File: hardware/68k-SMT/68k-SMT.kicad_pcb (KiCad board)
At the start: 2 copper layers, 106.7 x 139.7 mm, 67 parts, among them J1 ADBUS, J3 SIGBUS, J4 Serial1, J5 Serial2, J6 CompactFlash, SW1 RESET, SW2 IP2, SW3 IP3, U1 74HC32, U10 HM628512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

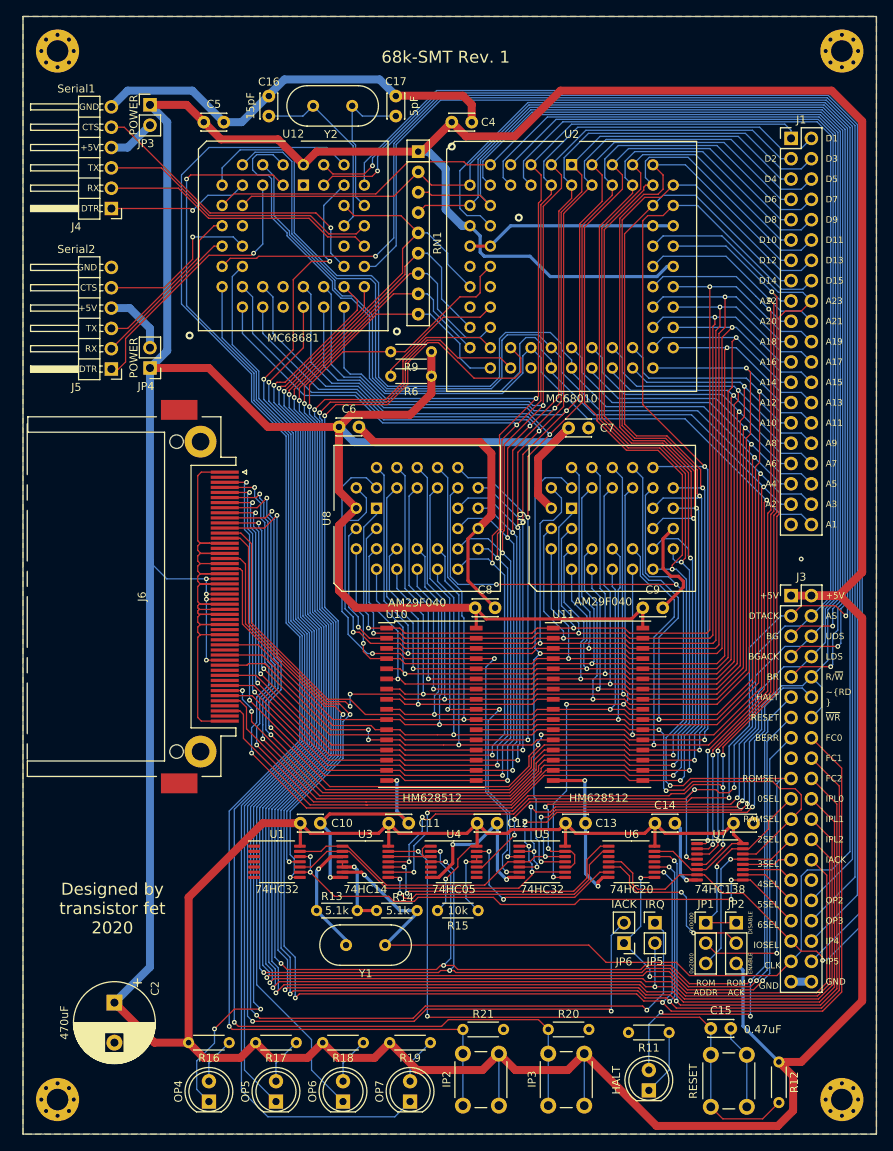
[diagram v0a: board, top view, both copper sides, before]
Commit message: Removed IDE header which doesn't easily fit, and cleaned up the PCB design a bit
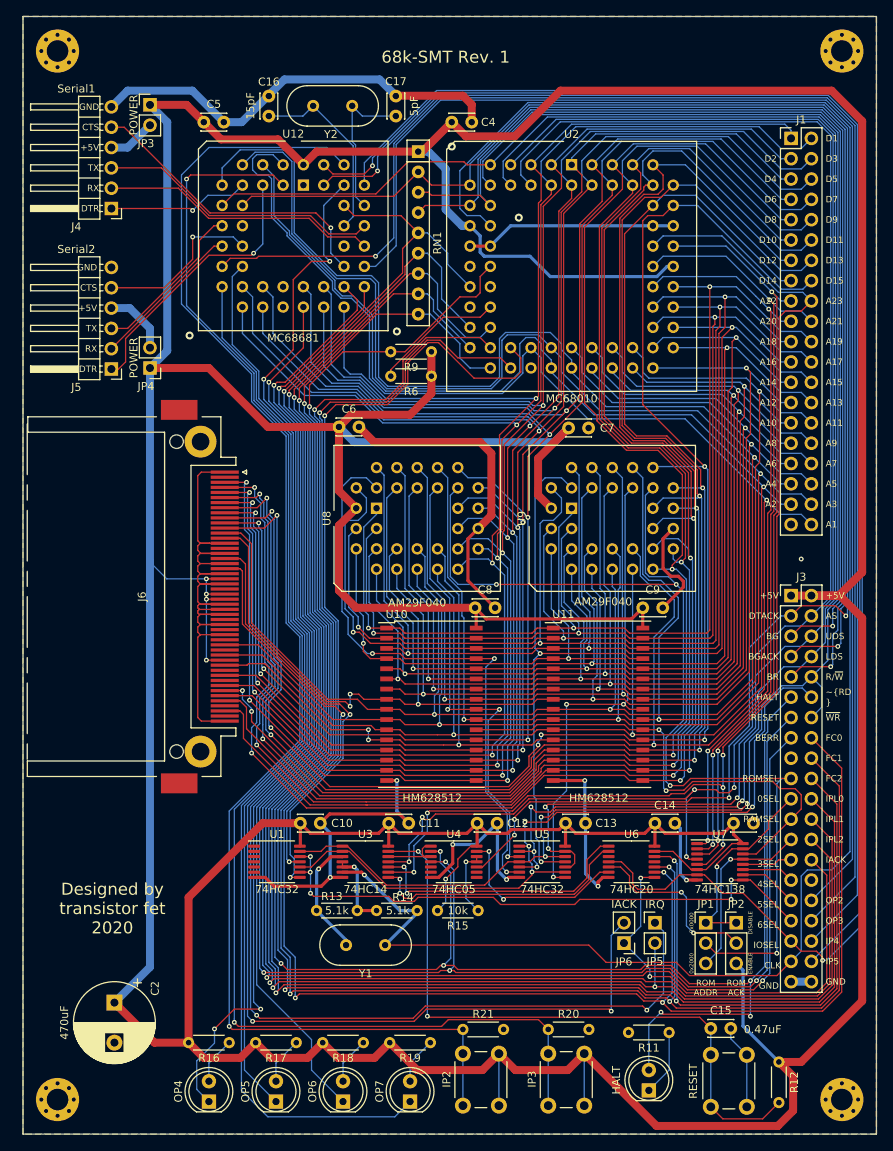
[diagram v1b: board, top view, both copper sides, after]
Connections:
- J6 pad 32: A12 -> A5
- J6 pad 7: A11 -> A4
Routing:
- net A11: track 216.6 -> 171.3 mm
- net A12: track 199.8 -> 156.3 mm, vias 5 -> 3
- net A5: track 155.8 -> 192.1 mm, vias 3 -> 5
- net A4: track 227.1 -> 262.3 mm
- net GND: track 314.7 -> 325.1 mm
- net 6SEL: track 71.6 -> 73.1 mm, vias 4 -> 5
- net D11: track 217.5 -> 218.6 mm
- net D9: track 182.0 -> 183.1 mm
- net D5: track 227.6 -> 228.4 mm
- net D7: track 224.7 -> 225.5 mm
- net D4: track 220.5 -> 221.2 mm
- net D10: track 183.2 -> 183.8 mm
- net D1: track 200.0 -> 200.5 mm

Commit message: Finalized 68k-SMT board and sent off to print
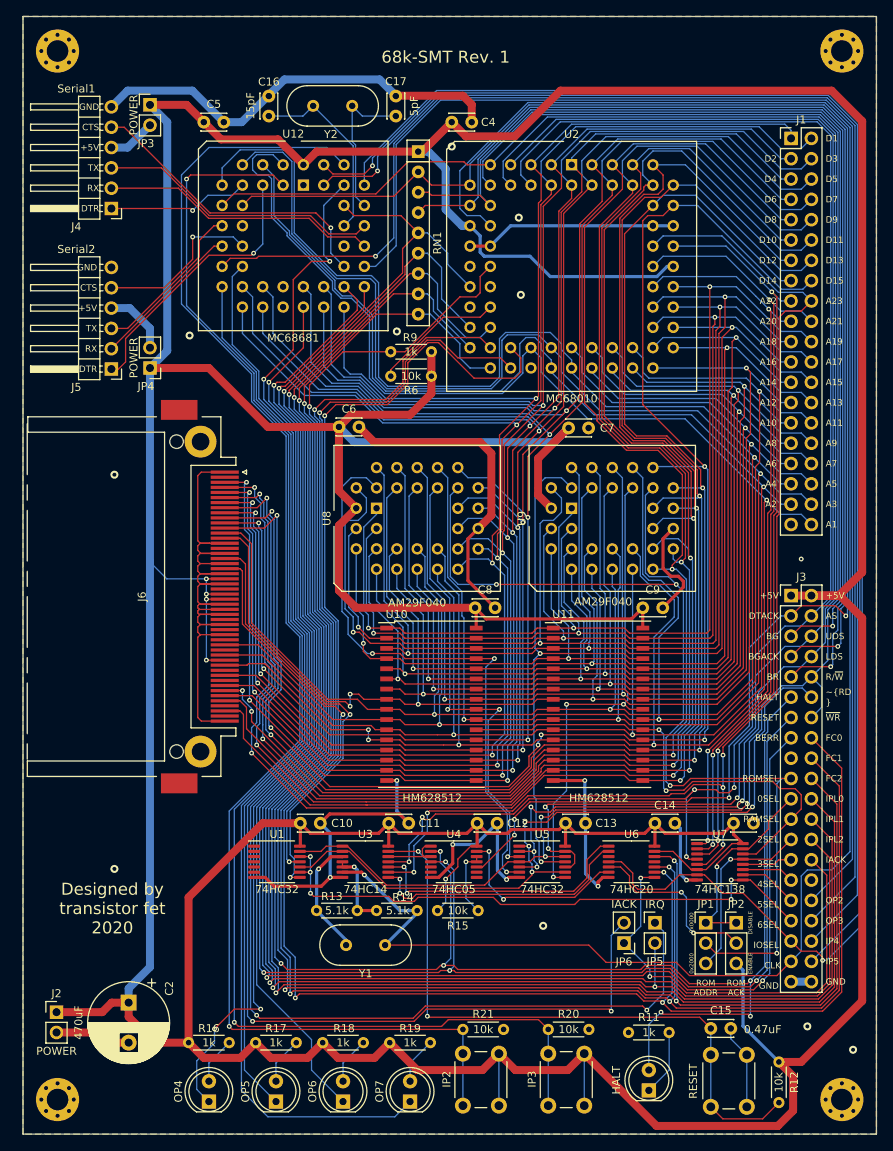
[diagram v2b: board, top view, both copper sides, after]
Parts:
- added J2: POWER, Connector_PinHeader_2.54mm:PinHeader_1x02_P2.54mm_Vertical, F.Cu at (108.3, 147.1)
- moved C2 1.78 mm to (117.3, 145.9)
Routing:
- net GND: track 325.1 -> 334.7 mm, vias 12 -> 18
- net +5V: track 847.0 -> 855.0 mm
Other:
- rule pad_to_mask_clearance: 0.051 -> 0.05
- rule solder_mask_min_width: 0.25 -> 0.1

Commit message: Upgraded project formats to kicad 6.0
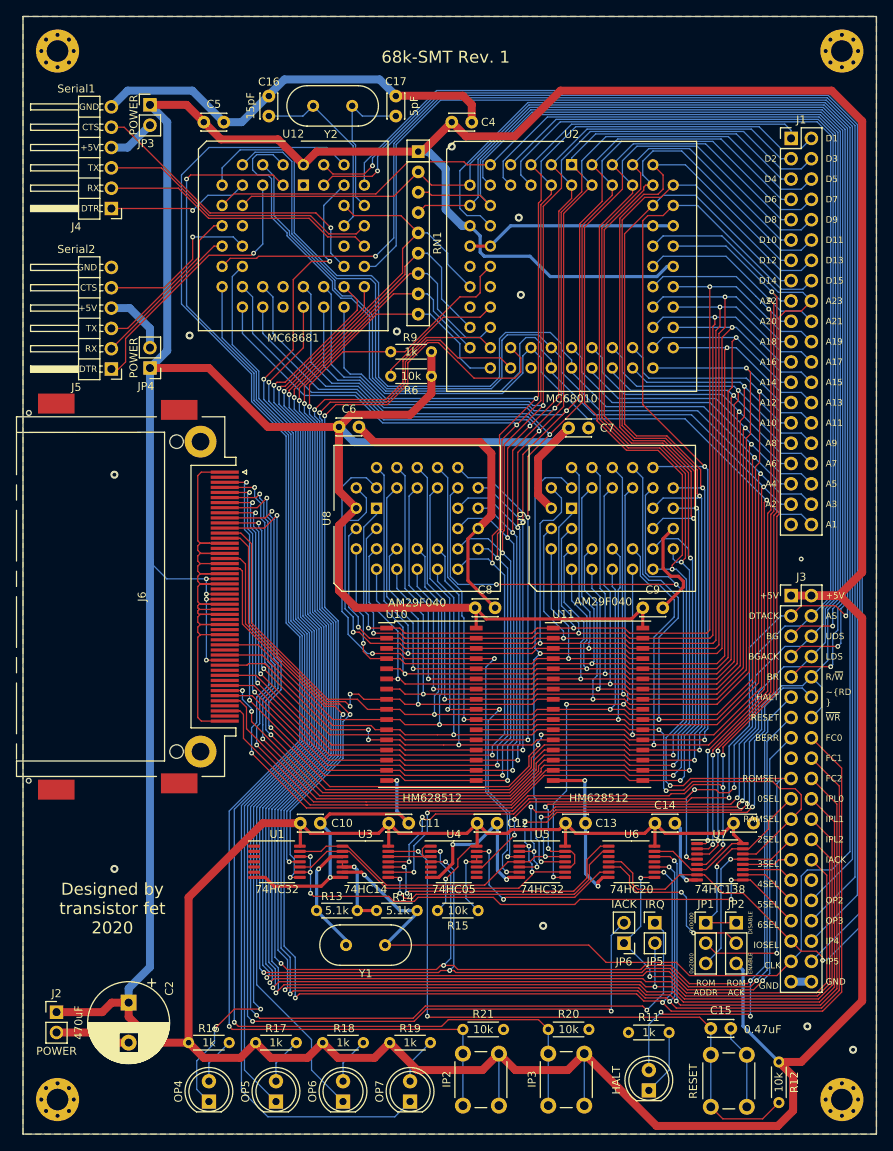
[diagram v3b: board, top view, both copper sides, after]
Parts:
- J6: footprint 68k-SMT:CF-Card_3M_N7E50-Q516RB-40 -> Computie_Connectors:CF-Card_3M_N7E50-Q516RB-40
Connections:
- net R~W renamed R~{W}
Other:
- net class Default removed
- board text added: "R/~{W}"
- board text added: "~{RD }"
- board text added: "~{WR}"
- board text removed: "R/~W"
- board text removed: "~RD"
- board text removed: "~WR"

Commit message: k30-SBC Revision 2 is complete
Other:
- board text added: "D0"
- board text added: "~{RD}"
- board text removed: "~{RD }"
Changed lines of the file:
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@@
     (effects (font (size 0.8 0.8) (thickness 0.15)) (justify left))
   )
-  (gr_text "~{RD\n}" (at 204.47 107.696) (layer "F.SilkS")
+  (gr_text "~{RD}" (at 204.47 107.696) (layer "F.SilkS")
     (effects (font (size 0.8 0.8) (thickness 0.15)) (justify left))
   )
@@
     (effects (font (size 1.5 1.5) (thickness 0.3)))
   )
+  (gr_text "D0" (at 198.247 37.846) (layer "F.SilkS")
+    (effects (font (size 0.8 0.8) (thickness 0.15)) (justify right))
+  )
   (segment (start 174.371 118.11) (end 174.371 118.11) (width 0.4) (layer "F.Cu") (net 1))
